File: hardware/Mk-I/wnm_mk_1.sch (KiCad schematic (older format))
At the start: 34 parts, among them SW1 EVQ-Q2S02W, SW10 EVQ-Q2S02W, SW11 EVQ-Q2S02W, SW12 EVQ-Q2S02W, SW13 EVQ-Q2S02W, SW14 EVQ-Q2S02W, SW15 EVQ-Q2S02W, SW16 EVQ-Q2S02W, SW18 EVQ-Q2S02W, SW19 EVQ-Q2S02W, SW2 EVQ-Q2S02W, SW20 EVQ-Q2S02W, SW21 EVQ-Q2S02W, SW22 EVQ-Q2S02W, SW3 EVQ-Q2S02W, SW4 EVQ-Q2S02W, SW5 EVQ-Q2S02W, SW6 EVQ-Q2S02W, SW7 EVQ-Q2S02W, SW8 EVQ-Q2S02W, SW9 EVQ-Q2S02W, U6 EC12D1524403, U7 EC12D1524403

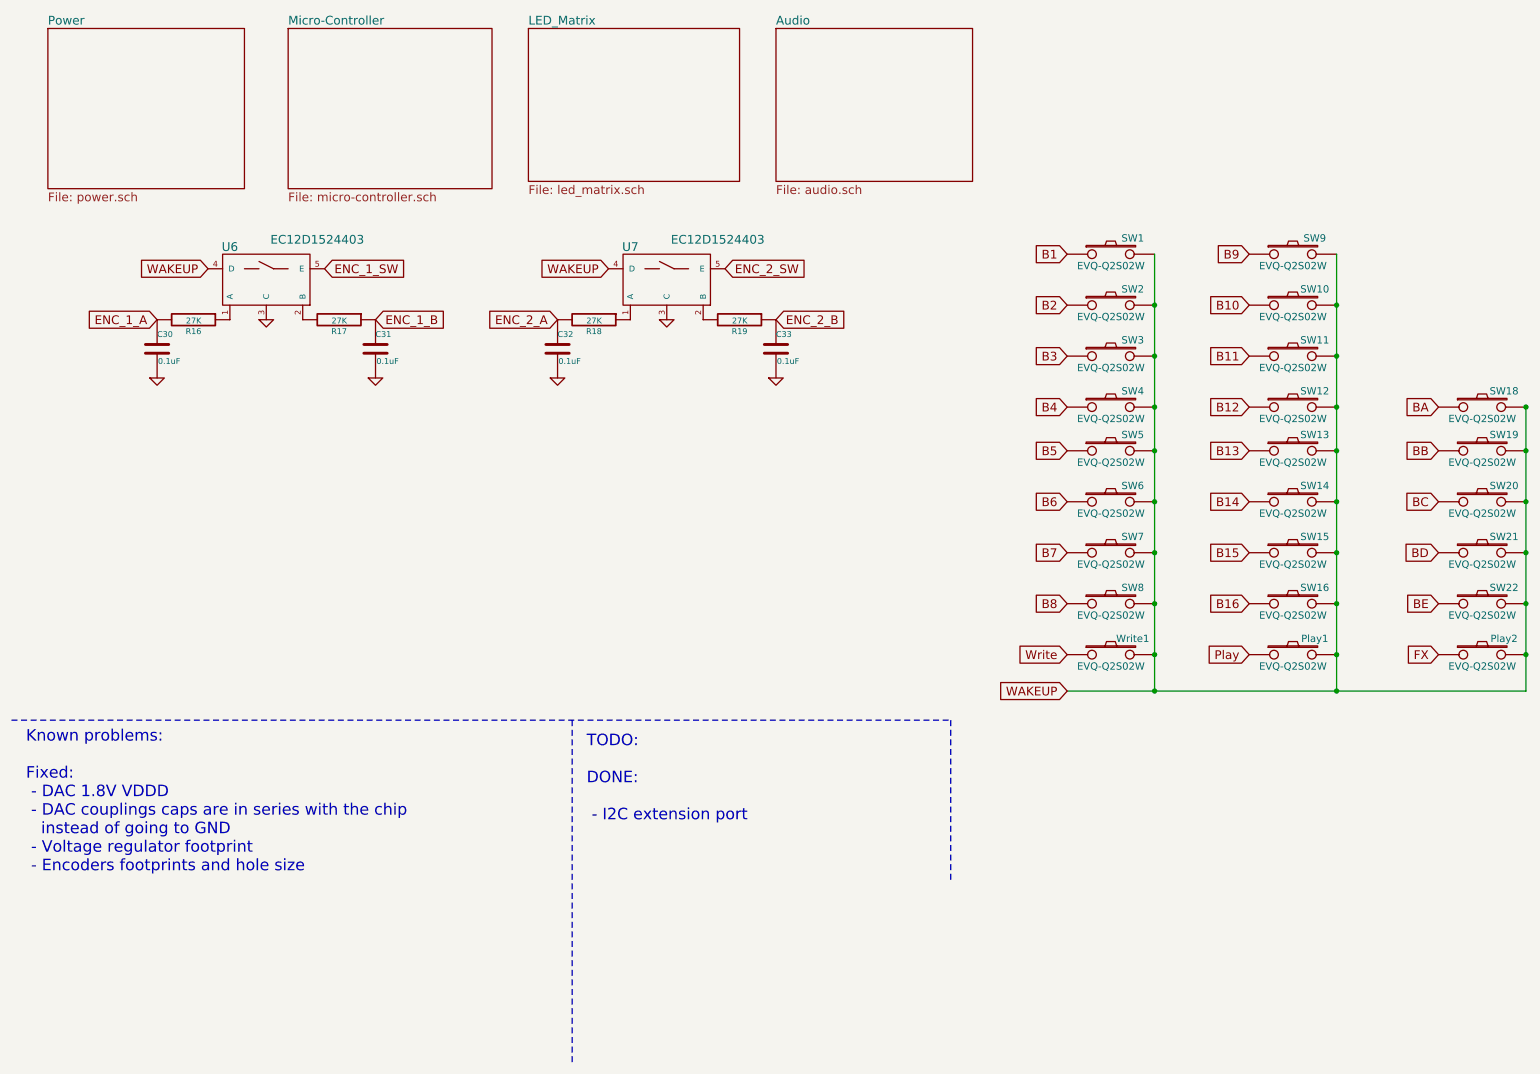
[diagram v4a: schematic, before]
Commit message: HW: TODO list for the next revision
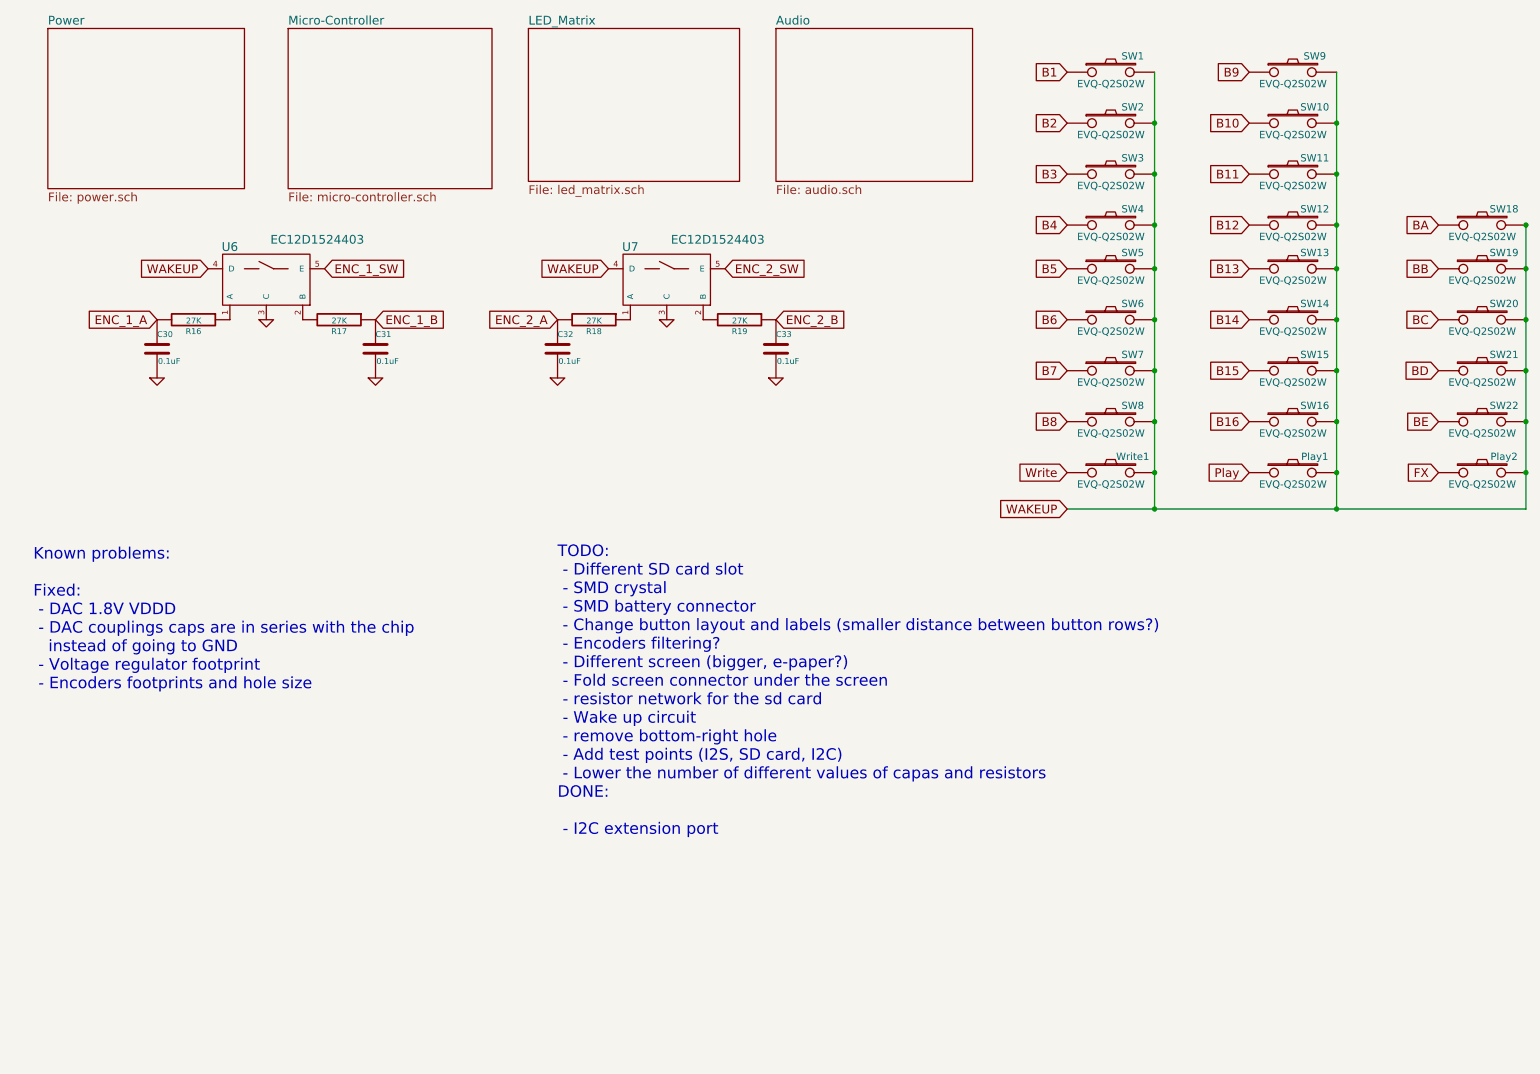
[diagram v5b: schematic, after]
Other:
- note added: "TODO:\n - Different SD card slot\n - SMD crystal\n - SMD battery connector\n - Change button layout and labels (smaller distance between button rows?)\n - Encoders filtering?\n - Different screen (bigger, e-paper?)\n - Fold screen connector under the screen\n - resistor network for the sd card\n - Wake up circuit\n - remove bottom-right hole\n - Add test points (I2S, SD card, I2C)\n - Lower the n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"
- note removed: "TODO:\n \nDONE:\n\n - I2C extension port"
- moved on the sheet: Play1, Play2, SW1, SW10, SW11, SW12, SW13, SW14, SW15, SW16, SW18, SW19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

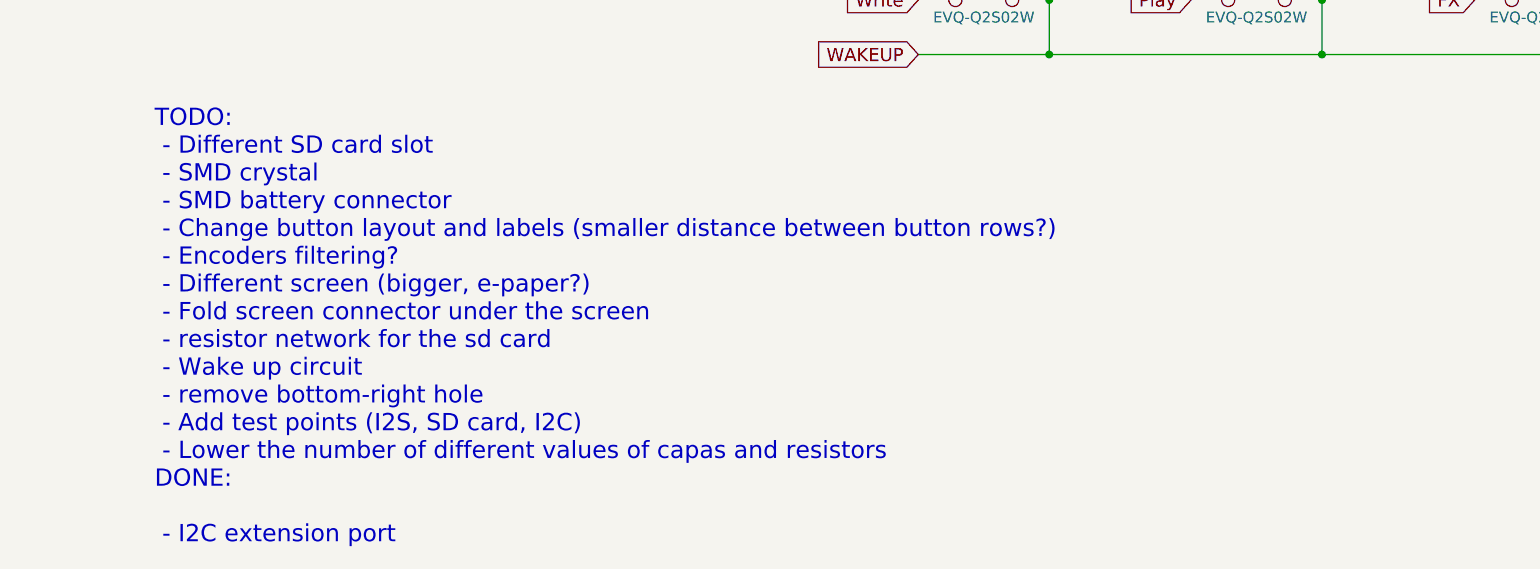
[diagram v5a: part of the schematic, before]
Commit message: HW: Change battery connector to SMD
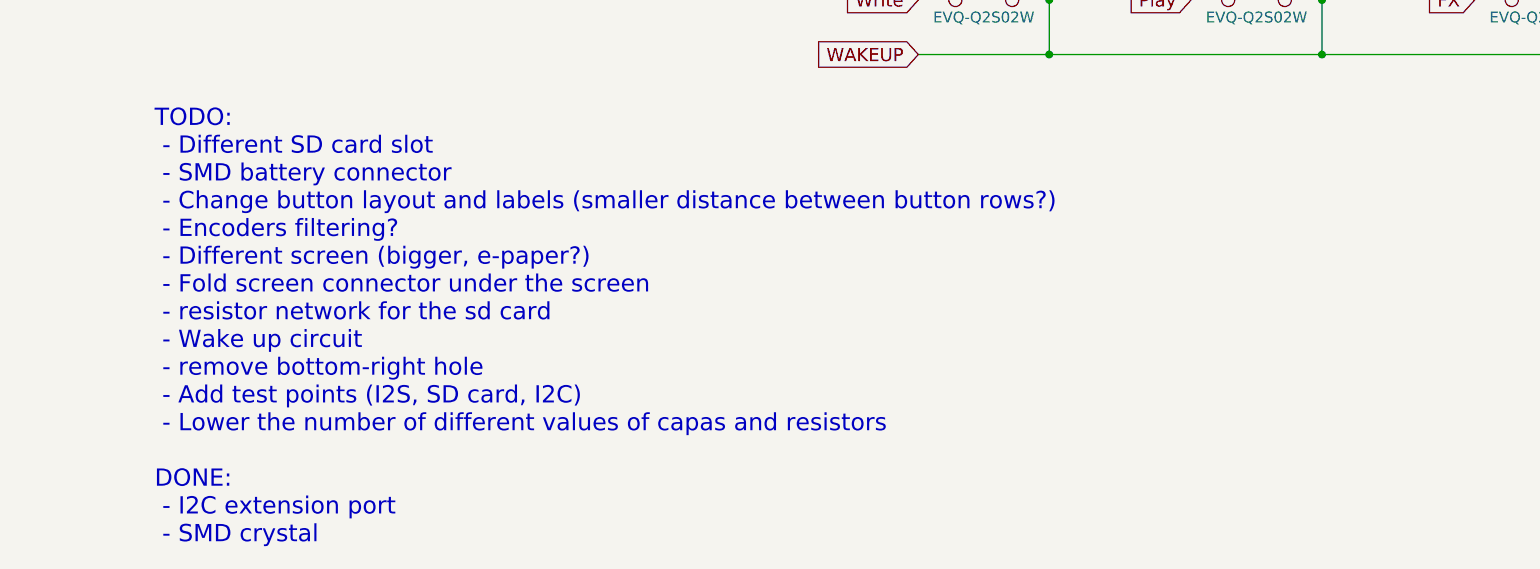
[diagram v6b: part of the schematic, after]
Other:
- note added: "TODO:\n - Different SD card slot\n - SMD battery connector\n - Change button layout and labels (smaller distance between button rows?)\n - Encoders filtering?\n - Different screen (bigger, e-paper?)\n - Fold screen connector under the screen\n - resistor network for the sd card\n - Wake up circuit\n - remove bottom-right hole\n - Add test points (I2S, SD card, I2C)\n - Lower the number of differe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"
- note removed: "TODO:\n - Different SD card slot\n - SMD crystal\n - SMD battery connector\n - Change button layout and labels (smaller distance between button rows?)\n - Encoders filtering?\n - Different screen (bigger, e-paper?)\n - Fold screen connector under the screen\n - resistor network for the sd card\n - Wake up circuit\n - remove bottom-right hole\n - Add test points (I2S, SD card, I2C)\n - Lower the n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"
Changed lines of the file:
@@
 $EndComp
 Text Notes 4250 6200 0    79   ~ 0
-TODO:\n - Different SD card slot\n - SMD crystal\n - SMD battery connector\n - Change button layout and labels (smaller distance between button rows?)\n - Encoders filtering?\n - Different screen (bigger, e-paper?)\n - Fold screen connector under the screen\n - resistor network for the sd card\n - Wake up circuit\n - remove bottom-right hole\n - Add test points (I2S, SD card, I2C)\n - Lower the number of different values of capas and resistors\nDONE:\n\n - I2C extension port
+TODO:\n - Different SD card slot\n - SMD battery connector\n - Change button layout and labels (smaller distance between button rows?)\n - Encoders filtering?\n - Different screen (bigger, e-paper?)\n - Fold screen connector under the screen\n - resistor network for the sd card\n - Wake up circuit\n - remove bottom-right hole\n - Add test points (I2S, SD card, I2C)\n - Lower the number of different values of capas and resistors\n\nDONE:\n - I2C extension port\n - SMD crystal\n
 Text Notes 650  5200 0    79   ~ 0
 Known problems:\n\nFixed:\n - DAC 1.8V VDDD\n - DAC couplings caps are in series with the chip \n   instead of going to GND\n - Voltage regulator footprint\n - Encoders footprints and hole size\n

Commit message: HW: Major change of layout...
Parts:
- removed C30, C31, C32, C33: 0.1uF, Capacitors_SMD:C_0805, symbol C-RESCUE-wnm_mk_1
- removed Play1, Play2, SW1, SW10, SW11, SW12, SW13, SW14, SW15, SW16, SW18, SW19, SW2, SW20, SW21, SW22, SW3, SW4, SW5, SW6, SW7, SW8, SW9, Write1: EVQ-Q2S02W, Buttons_Switches_SMD:SW_SPST_B3SL-1002P, symbol SW_PUSH
- removed R16, R17, R18, R19: 27K, Resistors_SMD:R_0805, symbol R-RESCUE-wnm_mk_1
- removed U6, U7: EC12D1524403, POSS:encoder_EC12D, symbol encoder_and_switch
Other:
- note added: "TODO:\n - Different SD card slot\n - Change button layout and labels (smaller distance between button rows?)\n - Encoders filtering?\n - Different screen (bigger, e-paper?)\n - Fold screen connector under the screen\n - resistor network for the sd card\n - Wake up circuit\n - remove bottom-right hole\n - Add test points (I2S, SD card, I2C)\n - Lower the number of different values of capas and res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"
- note removed: "TODO:\n - Different SD card slot\n - SMD battery connector\n - Change button layout and labels (smaller distance between button rows?)\n - Encoders filtering?\n - Different screen (bigger, e-paper?)\n - Fold screen connector under the screen\n - resistor network for the sd card\n - Wake up circuit\n - remove bottom-right hole\n - Add test points (I2S, SD card, I2C)\n - Lower the number of differe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"
